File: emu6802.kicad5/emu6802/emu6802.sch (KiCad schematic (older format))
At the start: 20 parts, among them CON1 Conn_01x08, CON2 Conn_01x06, J3 Barrel_Jack_Switch, U1 PIC18F47Q84-DIP40, U2 MC6802

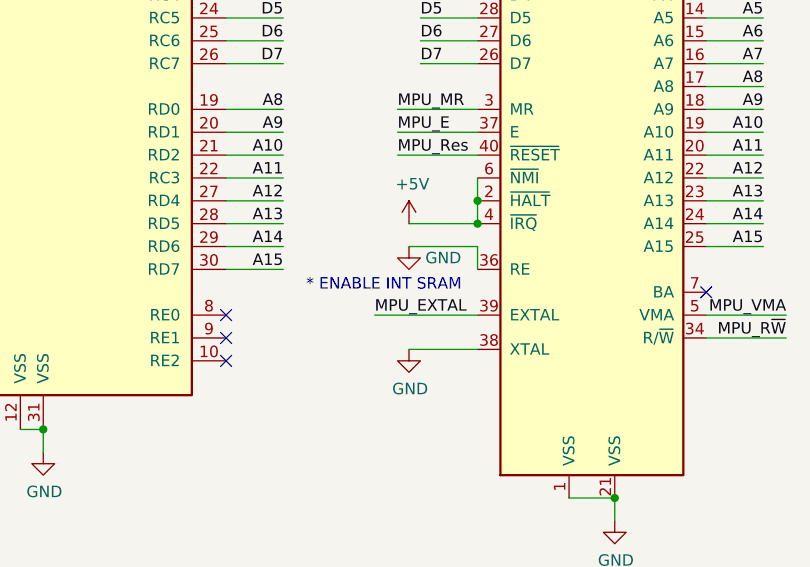
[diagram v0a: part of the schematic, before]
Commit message: update schematic
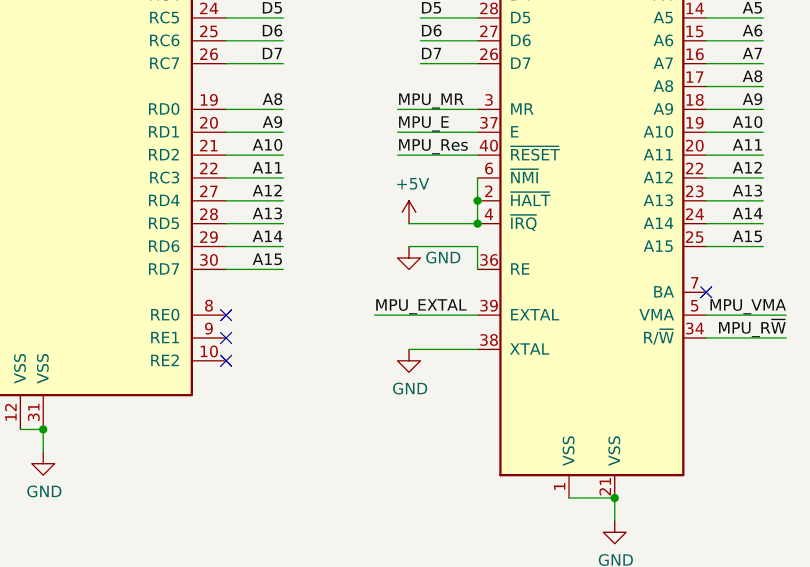
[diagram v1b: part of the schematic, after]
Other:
- note removed: "* ENABLE INT SRAM"
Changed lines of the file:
@@
 Wire Wire Line
 	9700 3500 9700 3650
-Text Notes 4000 4650 0    50   ~ 0
-* ENABLE INT SRAM
 $Comp
 L power:GND #PWR?

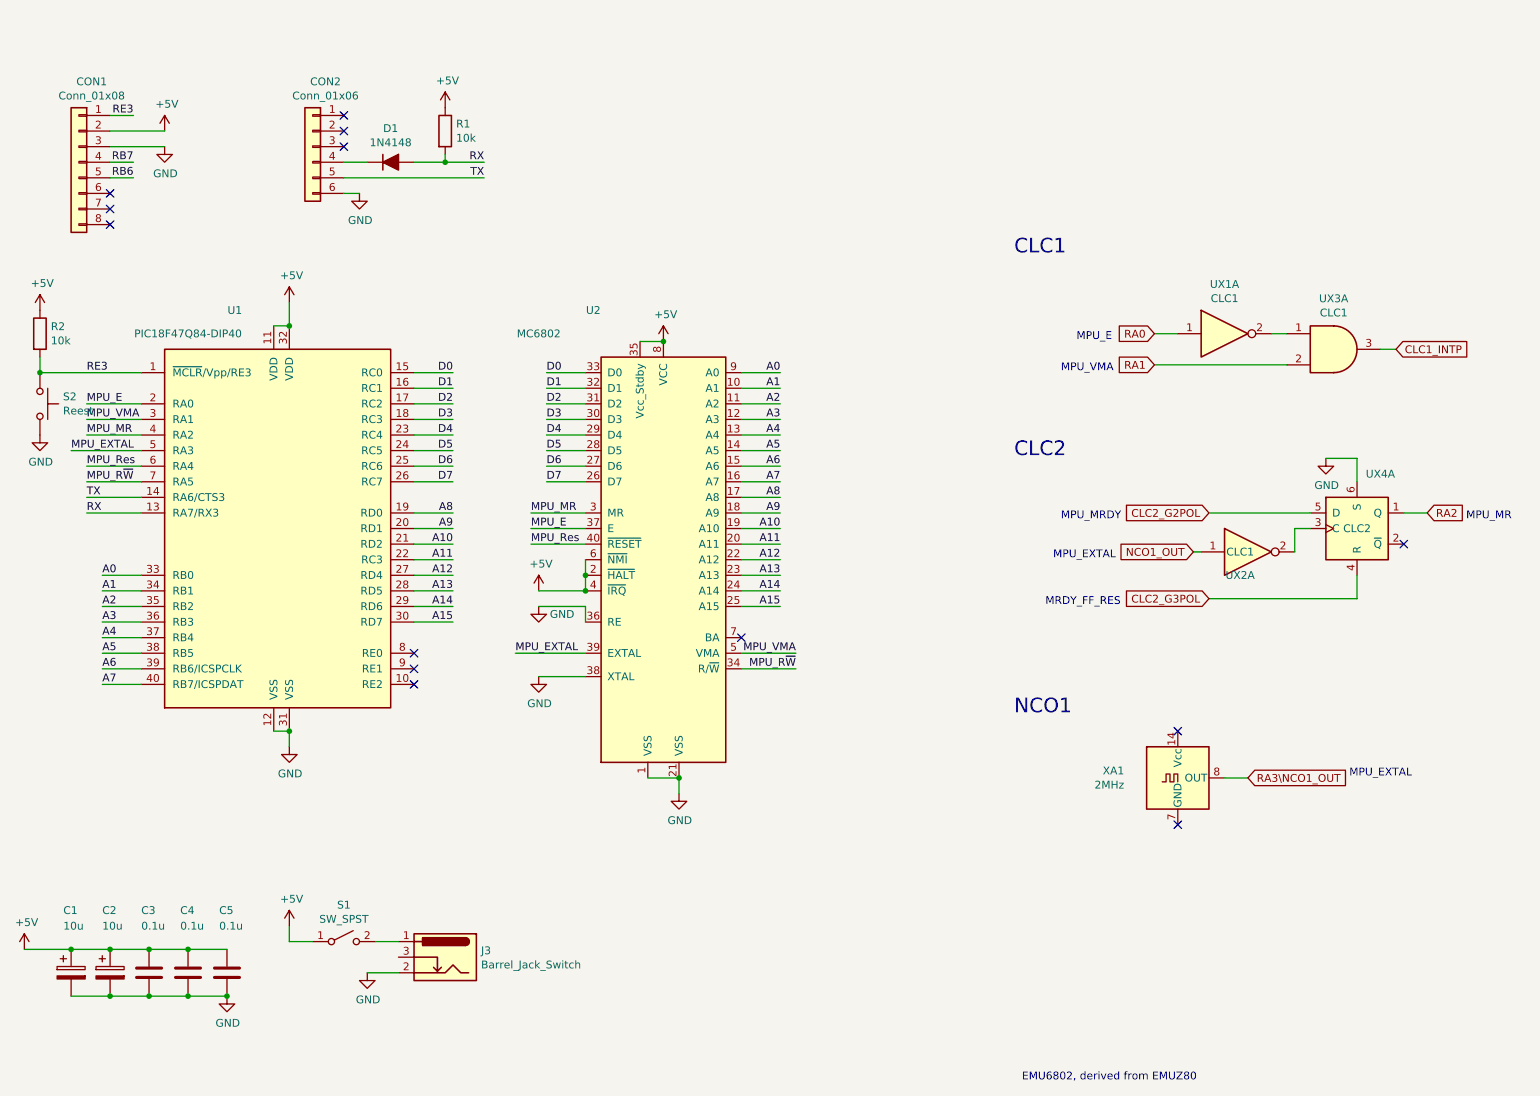
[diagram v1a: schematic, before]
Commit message: init irq branch working
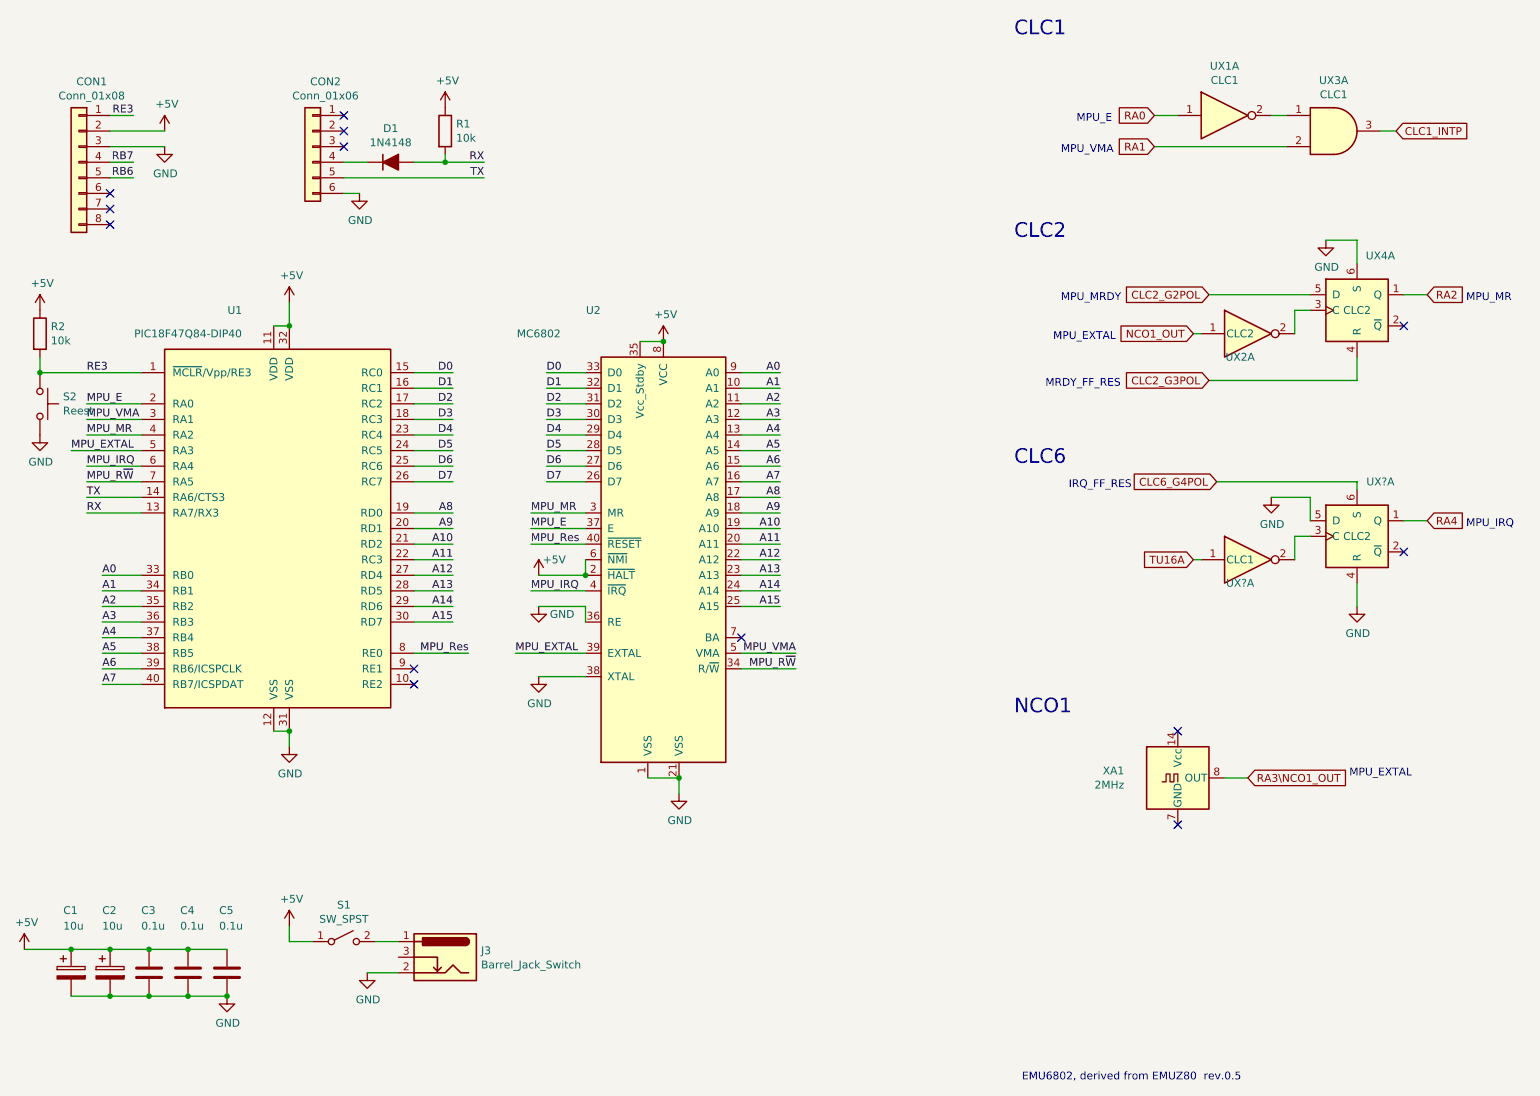
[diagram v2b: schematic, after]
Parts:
- added UX?: CLC2, symbol 4xxx:4013
- added UX?: CLC1, symbol 74xx:74LS04
- UX2: value CLC1 -> CLC2
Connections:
- net +5V: no longer U2.4 (~IRQ)
- net GND: now also UX?.4 (R), UX?.5 (D)
- net MPU_Res: now also U1.8 (RE0); no longer U1.6 (RA4)
- new net: UX?.2, UX?.3 (C)
- new net CLC6_G4POL: UX?.6 (S)
- new net MPU_IRQ: U1.6 (RA4), U2.4 (~IRQ)
- new net RA4: UX?.1 (Q)
- new net TU16A: UX?.1
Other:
- note added: "CLC6"
- note added: "EMU6802, derived from EMUZ80 rev.0.5"
- note added: "IRQ_FF_RES"
- note added: "MPU_IRQ"
- note removed: "EMU6802, derived from EMUZ80"
- moved on the sheet: UX1A, UX2A, UX3A, UX4A
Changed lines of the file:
@@
 	1900 3550 1550 3550
 Text Label 1550 3550 0    50   ~ 0
-MPU_Res
+MPU_IRQ
 Wire Wire Line
 	3650 3650 3900 3650
@@
 L power:+5V #PWR013
 U 1 1 62D778D7
-P 4450 4350
-F 0 "#PWR013" H 4450 4200 50  0001 C CNN
-F 1 "+5V" H 4465 4523 50  0000 C CNN
-F 2 "" H 4450 4350 50  0001 C CNN
-F 3 "" H 4450 4350 50  0001 C CNN
-	1    4450 4350
+P 4450 4250
+F 0 "#PWR013" H 4450 4100 50  0001 C CNN
+F 1 "+5V" H 4550 4350 50  0000 C CNN
+F 2 "" H 4450 4250 50  0001 C CNN
+F 3 "" H 4450 4250 50  0001 C CNN
+	1    4450 4250
 	1    0    0    -1
 $EndComp
@@
 	4750 4150 4750 4250
 Connection ~ 4750 4250
-Wire Wire Line
-	4750 4250 4750 4350
-Wire Wire Line
-	4450 4350 4750 4350
-Connection ~ 4750 4350
 NoConn ~ 5750 4650
-NoConn ~ 3650 4750
 NoConn ~ 3650 4850
 NoConn ~ 3650 4950
@@
 L 4xxx:4013 UX4
 U 1 1 62EFFDB6
-P 9700 3950
-F 0 "UX4" H 9850 4300 50  0000 C CNN
-F 1 "CLC2" H 9700 3950 50  0000 C CNN
-F 2 "" H 9700 3950 50  0001 C CNN
-F 3 "http://www.onsemi.com/pub/Collateral/MC14013B-D.PDF" H 9700 3950 50  0001 C CNN
-	1    9700 3950
+P 9700 2550
+F 0 "UX4" H 9850 2900 50  0000 C CNN
+F 1 "CLC2" H 9700 2550 50  0000 C CNN
+F 2 "" H 9700 2550 50  0001 C CNN
+F 3 "http://www.onsemi.com/pub/Collateral/MC14013B-D.PDF" H 9700 2550 50  0001 C CNN
+	1    9700 2550
 	1    0    0    -1
 $EndComp
@@
 L 4xxx:4081 UX3
 U 1 1 62F00D8C
-P 9550 2800
-F 0 "UX3" H 9550 3125 50  0000 C CNN
-F 1 "CLC1" H 9550 3034 50  0000 C CNN
-F 2 "" H 9550 2800 50  0001 C CNN
-F 3 "http://www.intersil.com/content/dam/Intersil/documents/cd40/cd4073bms-81bms-82bms.pdf" H 9550 2800 50  0001 C CNN
-	1    9550 2800
+P 9550 1400
+F 0 "UX3" H 9550 1725 50  0000 C CNN
+F 1 "CLC1" H 9550 1634 50  0000 C CNN
+F 2 "" H 9550 1400 50  0001 C CNN
+F 3 "http://www.intersil.com/content/dam/Intersil/documents/cd40/cd4073bms-81bms-82bms.pdf" H 9550 1400 50  0001 C CNN
+	1    9550 1400
 	1    0    0    -1
 $EndComp
@@
 L 74xx:74LS04 UX1
 U 1 1 62F0464B
-P 8850 2700
-F 0 "UX1" H 8850 3017 50  0000 C CNN
-F 1 "CLC1" H 8850 2926 50  0000 C CNN
-F 2 "" H 8850 2700 50  0001 C CNN
-F 3 "http://www.ti.com/lit/gpn/sn74LS04" H 8850 2700 50  0001 C CNN
-	1    8850 2700
-	1    0    0    -1
-$EndComp
-Wire Wire Line
-	9250 2700 9150 2700
-Wire Wire Line
-	10000 3850 10150 3850
-Text GLabel 10150 3850 2    50   Input ~ 0
+P 8850 1300
+F 0 "UX1" H 8850 1617 50  0000 C CNN
+F 1 "CLC1" H 8850 1526 50  0000 C CNN
+F 2 "" H 8850 1300 50  0001 C CNN
+F 3 "http://www.ti.com/lit/gpn/sn74LS04" H 8850 1300 50  0001 C CNN
+	1    8850 1300
+	1    0    0    -1
+$EndComp
+Wire Wire Line
+	9250 1300 9150 1300
+Wire Wire Line
+	10000 2450 10150 2450
+Text GLabel 10150 2450 2    50   Input ~ 0
 RA2
 $Comp
 L 74xx:74LS04 UX2
 U 1 1 62F26A3E
-P 9000 4100
-F 0 "UX2" H 8950 3950 50  0000 C CNN
-F 1 "CLC1" H 8950 4100 50  0000 C CNN
-F 2 "" H 9000 4100 50  0001 C CNN
-F 3 "http://www.ti.com/lit/gpn/sn74LS04" H 9000 4100 50  0001 C CNN
-	1    9000 4100
-	1    0    0    -1
-$EndComp
-Wire Wire Line
-	9400 3950 9300 3950
-Wire Wire Line
-	9300 3950 9300 4100
-Text GLabel 8650 4100 0    50   Input ~ 0
+P 9000 2700
+F 0 "UX2" H 8950 2550 50  0000 C CNN
+F 1 "CLC2" H 8950 2700 50  0000 C CNN
+F 2 "" H 9000 2700 50  0001 C CNN
+F 3 "http://www.ti.com/lit/gpn/sn74LS04" H 9000 2700 50  0001 C CNN
+	1    9000 2700
+	1    0    0    -1
+$EndComp
+Wire Wire Line
+	9400 2550 9300 2550
+Wire Wire Line
+	9300 2550 9300 2700
+Text GLabel 8650 2700 0    50   Input ~ 0
 NCO1_OUT
-Text GLabel 8400 2700 0    50   Input ~ 0
+Text GLabel 8400 1300 0    50   Input ~ 0
 RA0
-Text GLabel 8400 2900 0    50   Input ~ 0
+Text GLabel 8400 1500 0    50   Input ~ 0
 RA1
 Wire Wire Line
-	8550 2700 8400 2700
-Wire Wire Line
-	8400 2900 9250 2900
-Text GLabel 9950 2800 2    50   Input ~ 0
+	8550 1300 8400 1300
+Wire Wire Line
+	8400 1500 9250 1500
+Text GLabel 9950 1400 2    50   Input ~ 0
 CLC1_INTP
 Wire Wire Line
-	9850 2800 9950 2800
-Text GLabel 8750 3850 0    50   Input ~ 0
+	9850 1400 9950 1400
+Text GLabel 8750 2450 0    50   Input ~ 0
 CLC2_G2POL
 Wire Wire Line
-	8750 3850 9400 3850
-Text GLabel 8750 4400 0    50   Input ~ 0
+	8750 2450 9400 2450
+Text GLabel 8750 3000 0    50   Input ~ 0
 CLC2_G3POL
 Wire Wire Line
-	9700 4400 8750 4400
+	9700 3000 8750 3000
 $Comp
 L power:GND #PWR018
 U 1 1 62F727F3
-P 9500 3500
-F 0 "#PWR018" H 9500 3250 50  0001 C CNN
-F 1 "GND" H 9505 3327 50  0000 C CNN
-F 2 "" H 9500 3500 50  0001 C CNN
-F 3 "" H 9500 3500 50  0001 C CNN
-	1    9500 3500
-	1    0    0    -1
-$EndComp
-NoConn ~ 10000 4050
-Text Notes 7800 3900 0    50   ~ 0
+P 9500 2100
+F 0 "#PWR018" H 9500 1850 50  0001 C CNN
+F 1 "GND" H 9505 1927 50  0000 C CNN
+F 2 "" H 9500 2100 50  0001 C CNN
+F 3 "" H 9500 2100 50  0001 C CNN
+	1    9500 2100
+	1    0    0    -1
+$EndComp
+NoConn ~ 10000 2650
+Text Notes 7800 2500 0    50   ~ 0
 MPU_MRDY
-Text Notes 7750 4150 0    50   ~ 0
+Text Notes 7750 2750 0    50   ~ 0
 MPU_EXTAL
-Text Notes 7700 4450 0    50   ~ 0
+Text Notes 7700 3050 0    50   ~ 0
 MRDY_FF_RES
-Text Notes 7500 2200 0    94   ~ 0
+Text Notes 7500 800  0    94   ~ 0
 CLC1
-Text Notes 7500 3500 0    94   ~ 0
+Text Notes 7500 2100 0    94   ~ 0
 CLC2
 Text Notes 7500 5150 0    94   ~ 0
 NCO1
-Text Notes 10400 3900 0    50   ~ 0
+Text Notes 10400 2500 0    50   ~ 0
 MPU_MR
-Text Notes 7900 2750 0    50   ~ 0
+Text Notes 7900 1350 0    50   ~ 0
 MPU_E
-Text Notes 7800 2950 0    50   ~ 0
+Text Notes 7800 1550 0    50   ~ 0
 MPU_VMA
 $Comp
@@
 	9000 5550 8850 5550
 Wire Wire Line
-	8700 4100 8650 4100
+	8700 2700 8650 2700
 Text Notes 9650 5550 0    50   ~ 0
 MPU_EXTAL
 Text Notes 7550 7500 0    50   ~ 0
-EMU6802, derived from EMUZ80
-Wire Wire Line
-	9700 4400 9700 4250
-Wire Wire Line
-	9700 3500 9500 3500
-Wire Wire Line
-	9700 3500 9700 3650
+EMU6802, derived from EMUZ80  rev.0.5
+Wire Wire Line
+	9700 3000 9700 2850
+Wire Wire Line
+	9700 2100 9500 2100
+Wire Wire Line
+	9700 2100 9700 2250
 $Comp
 L power:GND #PWR?
@@
 Wire Wire Line
 	4750 4450 4750 4550
+$Comp
+L 4xxx:4013 UX?
+U 1 1 62FA01D8
+P 9700 4000
+F 0 "UX?" H 9850 4350 50  0000 C CNN
+F 1 "CLC2" H 9700 4000 50  0000 C CNN
+F 2 "" H 9700 4000 50  0001 C CNN
+F 3 "http://www.onsemi.com/pub/Collateral/MC14013B-D.PDF" H 9700 4000 50  0001 C CNN
+	1    9700 4000
+	1    0    0    -1
+$EndComp
+Wire Wire Line
+	10000 3900 10150 3900
+Text GLabel 10150 3900 2    50   Input ~ 0
+RA4
+$Comp
+L 74xx:74LS04 UX?
+U 1 1 62FA01E0
+P 9000 4150
+F 0 "UX?" H 8950 4000 50  0000 C CNN
+F 1 "CLC1" H 8950 4150 50  0000 C CNN
+F 2 "" H 9000 4150 50  0001 C CNN
+F 3 "http://www.ti.com/lit/gpn/sn74LS04" H 9000 4150 50  0001 C CNN
+	1    9000 4150
+	1    0    0    -1
+$EndComp
+Wire Wire Line
+	9400 4000 9300 4000
+Wire Wire Line
+	9300 4000 9300 4150
+Text GLabel 8650 4150 0    50   Input ~ 0
+TU16A
+Text GLabel 8800 3650 0    50   Input ~ 0
+CLC6_G4POL
+$Comp
+L power:GND #PWR?
+U 1 1 62FA01ED
+P 9150 3750
+F 0 "#PWR?" H 9150 3500 50  0001 C CNN
+F 1 "GND" H 9155 3577 50  0000 C CNN
+F 2 "" H 9150 3750 50  0001 C CNN
+F 3 "" H 9150 3750 50  0001 C CNN
+	1    9150 3750
+	1    0    0    -1
+$EndComp
+NoConn ~ 10000 4100
+Text Notes 7850 3700 0    50   ~ 0
+IRQ_FF_RES
+Text Notes 7500 3550 0    94   ~ 0
+CLC6
+Text Notes 10400 3950 0    50   ~ 0
+MPU_IRQ
+Wire Wire Line
+	8700 4150 8650 4150
+Wire Wire Line
+	9700 4450 9700 4300
+Wire Wire Line
+	8800 3650 9700 3650
+Wire Wire Line
+	9700 3650 9700 3700
+Wire Wire Line
+	9150 3750 9400 3750
+Wire Wire Line
+	9400 3750 9400 3900
+$Comp
+L power:GND #PWR?
+U 1 1 62FBA020
+P 9700 4450
+F 0 "#PWR?" H 9700 4200 50  0001 C CNN
+F 1 "GND" H 9705 4277 50  0000 C CNN
+F 2 "" H 9700 4450 50  0001 C CNN
+F 3 "" H 9700 4450 50  0001 C CNN
+	1    9700 4450
+	1    0    0    -1
+$EndComp
+Wire Wire Line
+	4750 4250 4450 4250
+Wire Wire Line
+	4400 4350 4750 4350
+Text Label 4400 4350 0    50   ~ 0
+MPU_IRQ
+Wire Wire Line
+	3650 4750 4000 4750
+Text Label 4000 4750 2    50   ~ 0
+MPU_Res
 $EndSCHEMATC
